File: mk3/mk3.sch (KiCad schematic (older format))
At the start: 191 parts, among them J1 JTAG, J2 USB_B_Micro, J3 Conn_01x04, SW1 BOOT, SW2 RESET, U1 STM32F070CBTx, U10 CHERRY_ML, U11 CHERRY_ML, U14 CHERRY_ML, U15 CHERRY_ML, U16 CHERRY_ML, U19 CHERRY_ML, U2 CHERRY_ML, U20 CHERRY_ML, U21 CHERRY_ML, U24 CHERRY_ML, U25 CHERRY_ML, U26 CHERRY_ML, U29 CHERRY_ML, U30 CHERRY_ML, U31 CHERRY_ML, U33 CHERRY_ML, U34 CHERRY_ML, U35 CHERRY_ML, U36 CHERRY_ML, U38 CHERRY_ML, U39 CHERRY_ML, U4 CHERRY_ML, U40 CHERRY_ML, U43 CHERRY_ML, U44 CHERRY_ML, U45 CHERRY_ML, U48 CHERRY_ML, U49 CHERRY_ML, U5 CHERRY_ML, U50 CHERRY_ML, U51 CHERRY_ML, U53 CHERRY_ML, U54 CHERRY_ML, U55 CHERRY_ML, U56 CHERRY_ML, U58 CHERRY_ML, U59 CHERRY_ML, U6 CHERRY_ML, U60 CHERRY_ML, U61 CHERRY_ML, U7 CHERRY_ML, U9 CHERRY_ML, X1 8 MHz

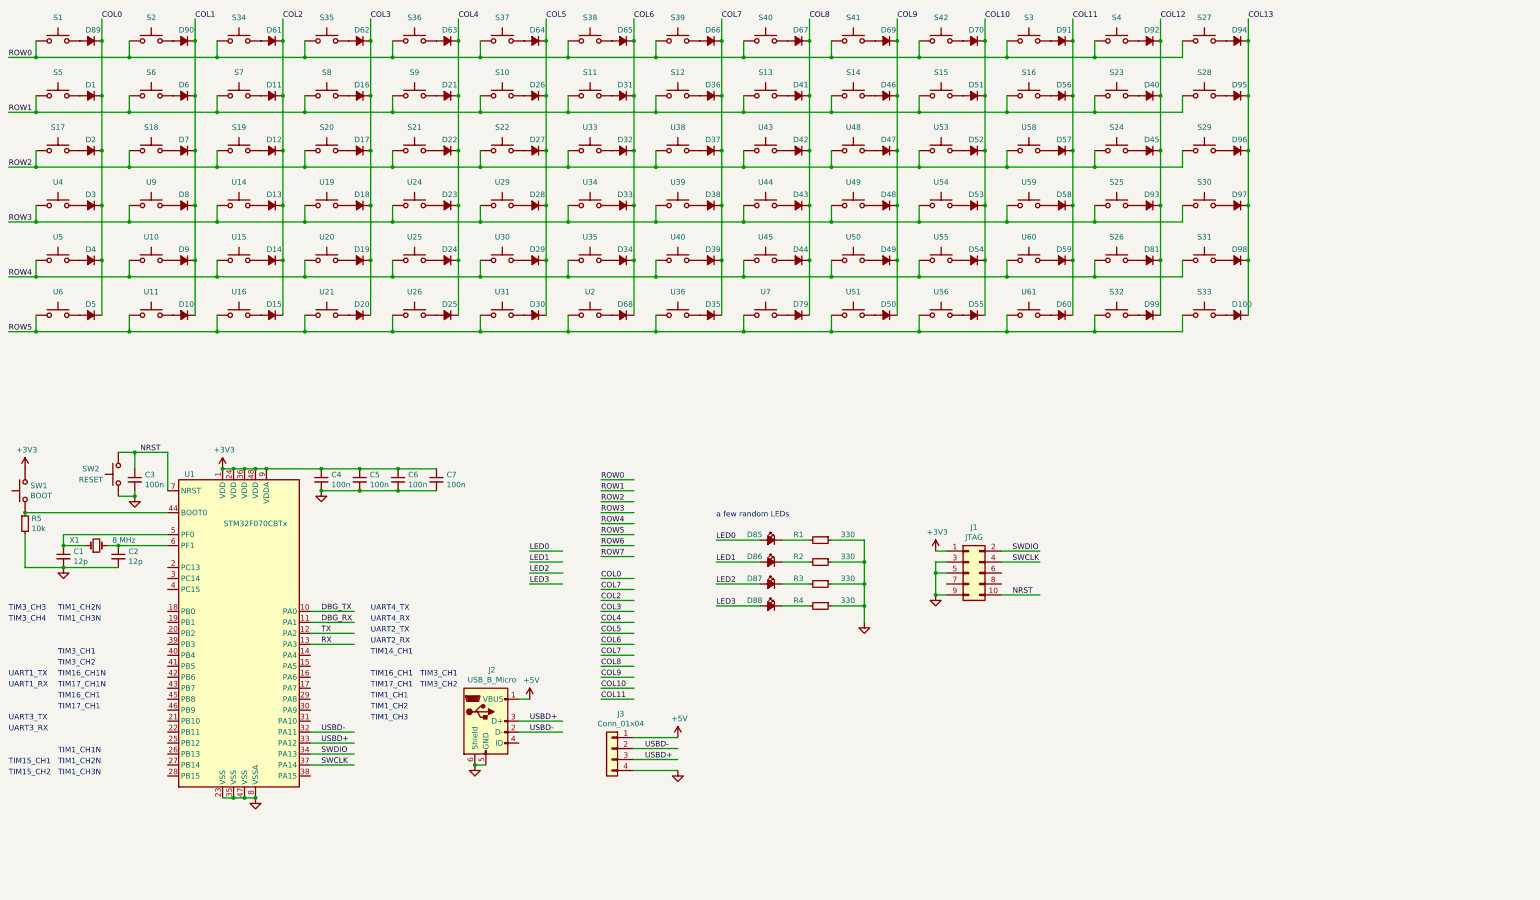
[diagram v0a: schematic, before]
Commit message: add another key column to left side of layout
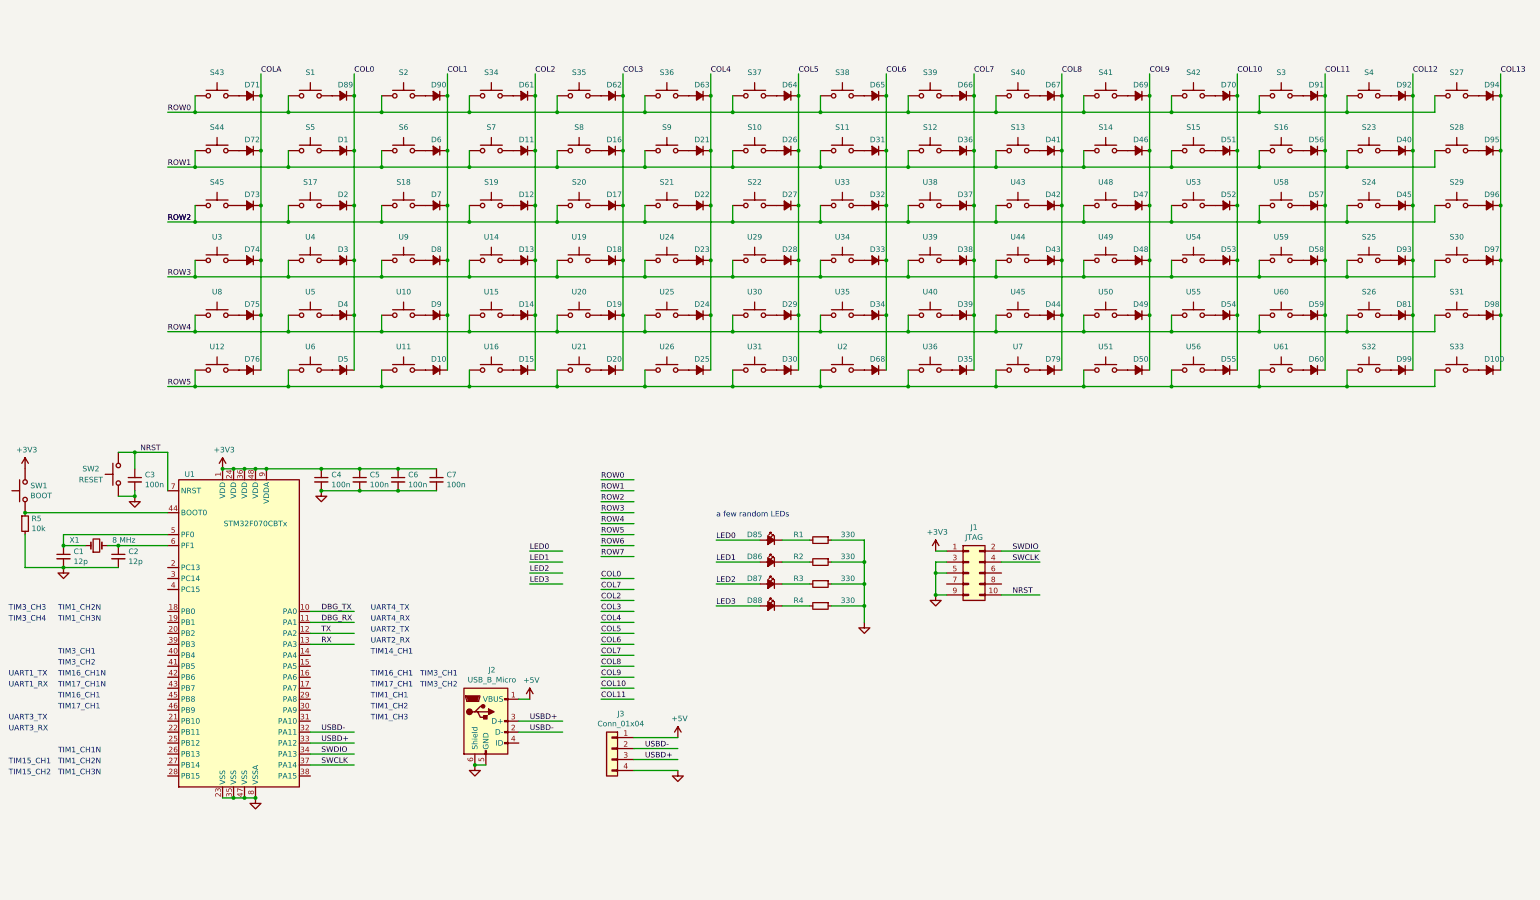
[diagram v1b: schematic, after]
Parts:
- added D71, D72, D73, D74, D75, D76: 1N4148, Diode_SMD:D_SOD-123, symbol Device:D_Small_ALT
- added S43, S44, S45, U12, U3, U8: CHERRY_ML, Switches:KAILH_1350, symbol Switch:SW_Push
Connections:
- net labels added: COLA
- wire segments 346 -> 364
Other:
- moved on the sheet: D1, D10, D100, D11, D12, D13, D14, D15, D16, D17, D18, D19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

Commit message: route a few columns of keys
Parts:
- S1, S10, S11, S12, S13, S14, S15, S16, S17, S18, S19, S2, S20, S21, S22, S23, S24, S25, S26, S27, S28, S29, S3, S30, S31, S32, S33, S34, S35, S36, S37, S38, S39, S4, S40, S41, S42, S43, S44, S45, S5, S6, S7, S8, S9, U10, U11, U12, U14, U15, U16, U19, U2, U20, U21, U24, U25, U26, U29, U3, U30, U31, U33, U34, U35, U36, U38, U39, U4, U40, U43, U44, U45, U48, U49, U5, U50, U51, U53, U54, U55, U56, U58, U59, U6, U60, U61, U7, U8, U9: symbol Switch:SW_Push -> keyswitch:KAILH_1350
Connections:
- wire segments 364 -> 484

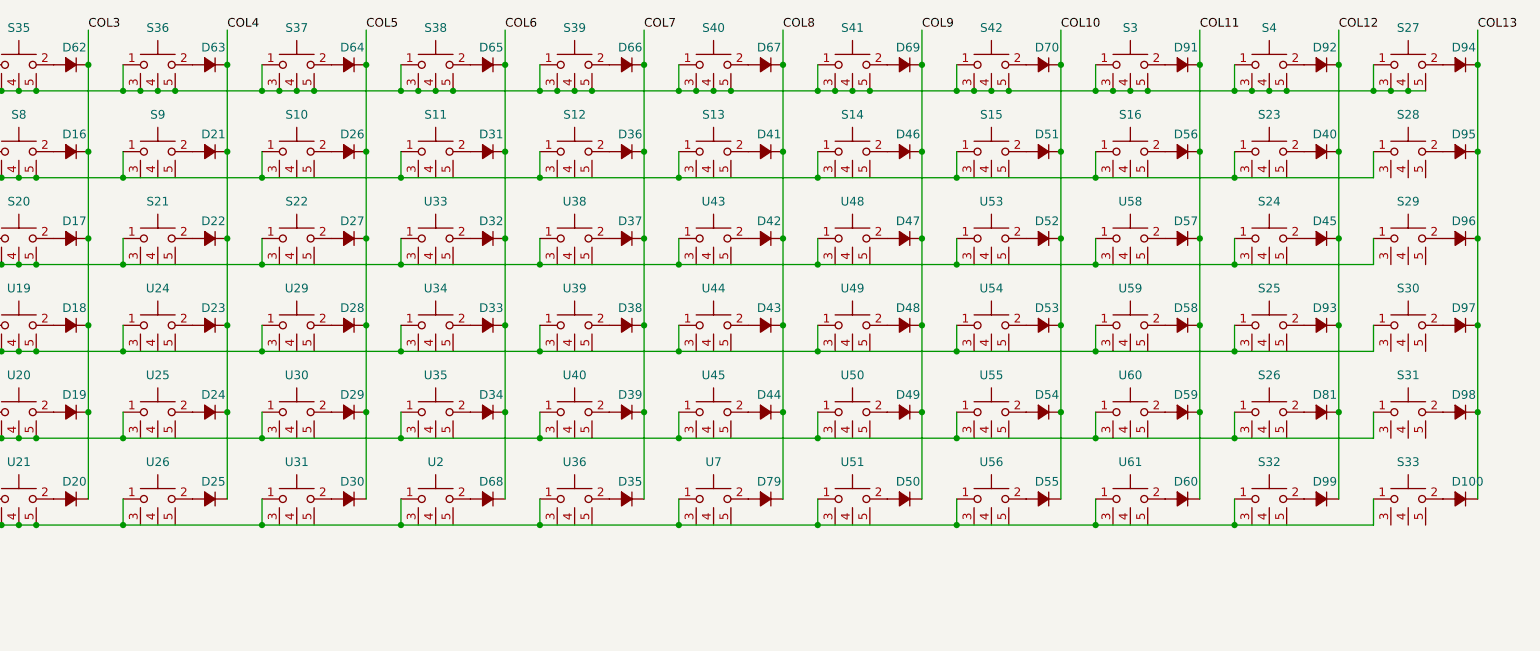
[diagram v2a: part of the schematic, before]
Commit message: place/route keyswitches and diodes
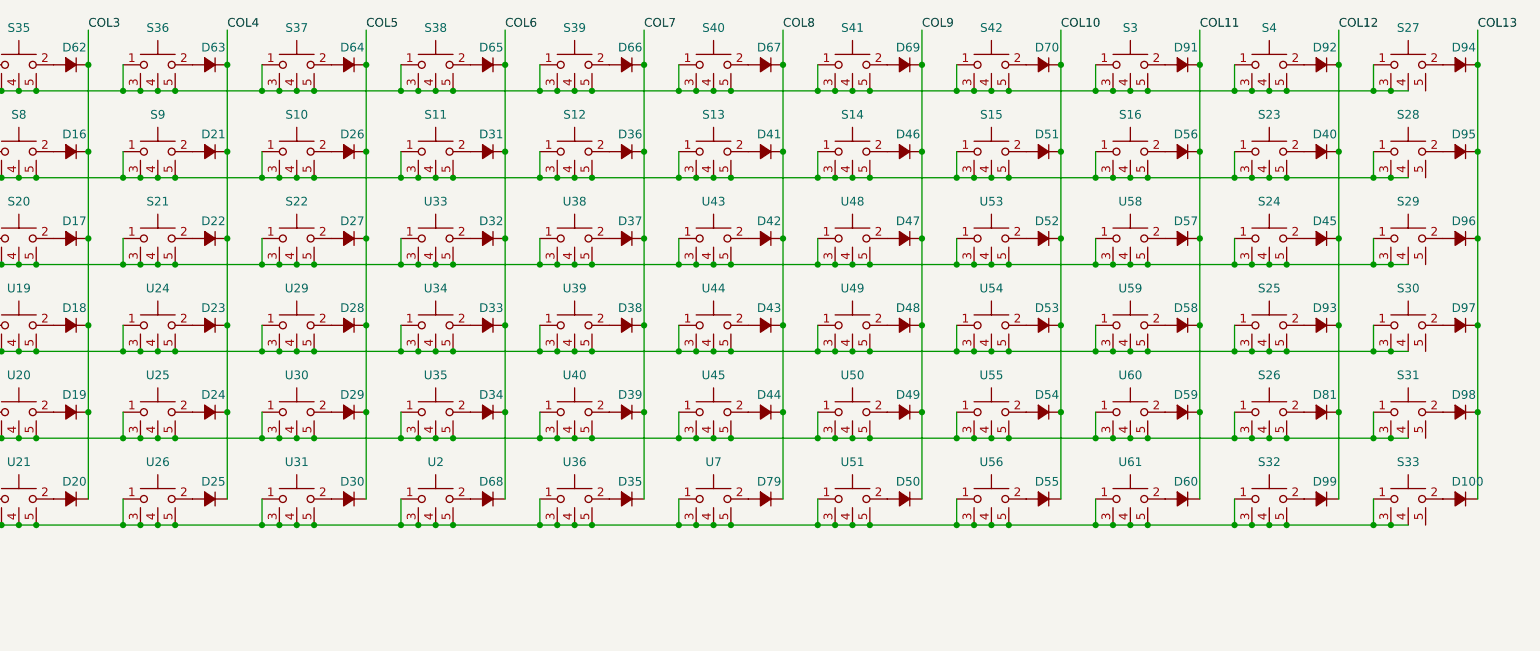
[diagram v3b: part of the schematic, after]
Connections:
- wire segments 484 -> 628

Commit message: a bit of place/route for the MCU section
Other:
- note added: "TODO: 3v3 LDO"
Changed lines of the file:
@@
 Wire Wire Line
 	5950 4900 6250 4900
-Text Label 5950 4800 0    50   ~ 0
+Text Label 1700 6900 0    50   ~ 0
 ROW0
 Wire Wire Line
-	5950 4800 6250 4800
+	1700 6900 2000 6900
 Text Label 5950 6400 0    50   ~ 0
 COL7
@@
 Wire Wire Line
 	5950 5700 6250 5700
-Text Label 5950 6800 0    50   ~ 0
+Text Label 1700 6800 0    50   ~ 0
 COL11
 Wire Wire Line
-	5950 6800 6250 6800
+	1700 6800 2000 6800
 Text Label 5950 6700 0    50   ~ 0
 COL10
@@
 Wire Wire Line
 	13650 3950 13750 3950
+Text Notes 8250 7350 0    118  ~ 24
+TODO: 3v3 LDO
 $EndSCHEMATC

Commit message: finish first attempt at place and route
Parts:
- removed D86, D87, D88: LED_Small_ALT, LED_THT:LED_D3.0mm, symbol Device:LED_Small_ALT
- removed R2, R3, R4: 330, Resistor_SMD:R_0603_1608Metric, symbol Device:R_Small
- added C10: 10u, Capacitor_SMD:C_0805_2012Metric, symbol Device:C_Small
- added C8, C9: 100n, Capacitor_SMD:C_0603_1608Metric, symbol Device:C_Small
- added J4: DEBUG, Connector_PinHeader_2.54mm:PinHeader_2x03_P2.54mm_Vertical, symbol Connector_Generic:Conn_02x03_Odd_Even
- added U13: TPS70933, Package_TO_SOT_SMD:SOT-23-5, symbol Regulator_Linear:TLV70033_SOT23-5
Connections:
- net labels removed: LED1, LED2, LED3, ROW6, ROW7
- wire segments 628 -> 632
- no-connect marks 0 -> 1
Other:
- note removed: "TODO: 3v3 LDO"
- moved on the sheet: C1, C2, X1
